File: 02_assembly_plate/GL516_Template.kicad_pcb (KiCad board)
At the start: 2 copper layers, 304.4 x 98.8 mm, 87 parts, among them J1 Conn_01x02, SW1 SW_PUSH, SW10 SW_PUSH, SW11 SW_PUSH, SW12 SW_PUSH, SW13 SW_PUSH, SW14 SW_PUSH, SW15 SW_PUSH, SW16 SW_PUSH, SW17 SW_PUSH, SW18 SW_PUSH, SW19 SW_PUSH, SW2 SW_PUSH, SW20 SW_PUSH, SW21 SW_PUSH, SW22 SW_PUSH, SW23 SW_PUSH, SW24 SW_PUSH, SW25 SW_PUSH, SW26 SW_PUSH, SW27 SW_PUSH, SW28 SW_PUSH, SW29 SW_PUSH, SW3 SW_PUSH, SW30 SW_PUSH, SW31 SW_PUSH, SW32 SW_PUSH, SW33 SW_PUSH, SW34 SW_PUSH, SW35 SW_PUSH, SW36 SW_PUSH, SW37 SW_PUSH, SW38 SW_PUSH, SW39 SW_PUSH, SW4 SW_PUSH, SW40 SW_PUSH, SW41 SW_PUSH, SW42 SW_PUSH, SW43 SW_PUSH, SW5 SW_PUSH, SW6 SW_PUSH, SW7 SW_PUSH, SW8 SW_PUSH, SW9 SW_PUSH, U1 BLEMicroPro

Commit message: fix wiring
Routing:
- net GND: track 51.2 -> 115.7 mm
- net Col1: track 389.0 -> 393.3 mm
- net Col0: track 409.8 -> 407.7 mm
- net Row1: track 468.5 -> 470.5 mm
- net Net-(D9-Pad2): track 7.82 -> 9.86 mm
- net Row0: track 431.7 -> 432.8 mm, vias 1 -> 0
- net Col6: track 316.5 -> 315.5 mm

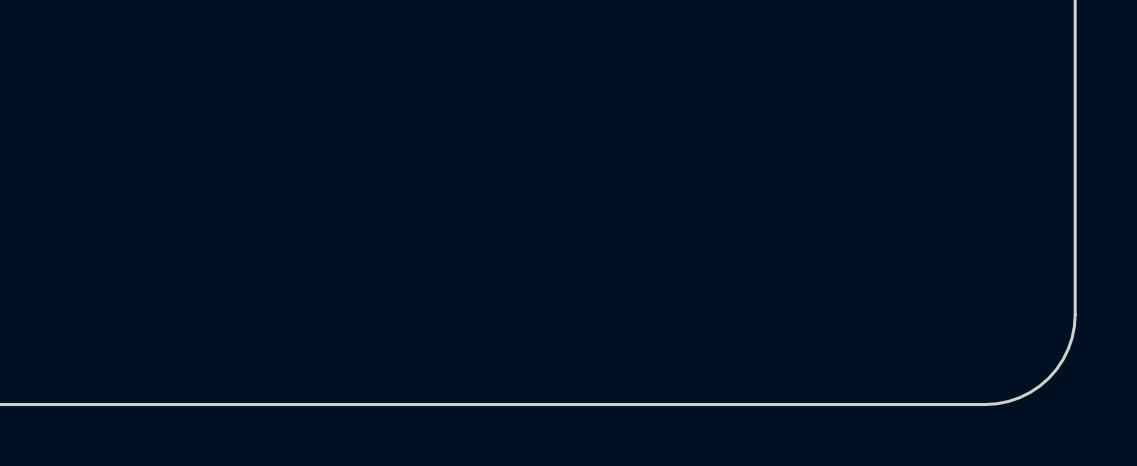
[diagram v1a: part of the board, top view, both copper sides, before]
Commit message: add version text on both Top and Assembly Plates
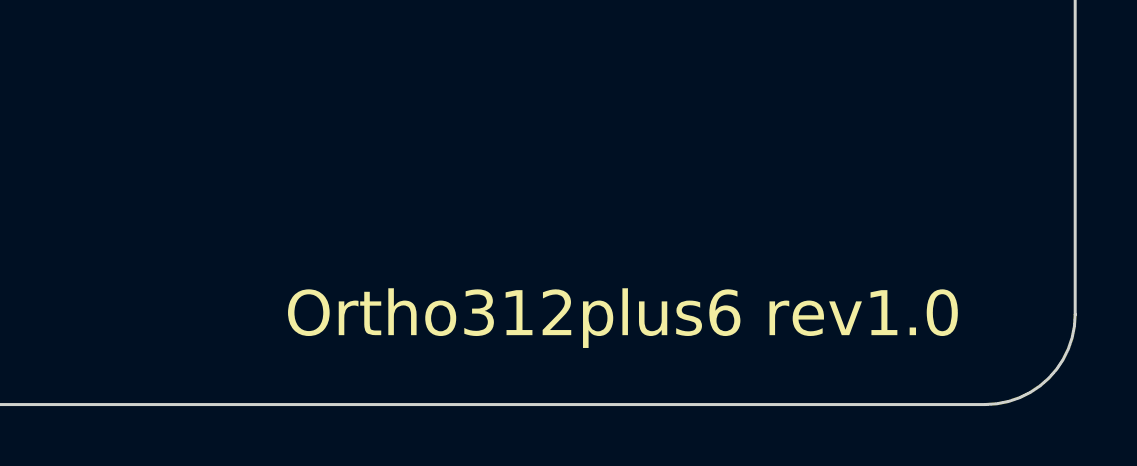
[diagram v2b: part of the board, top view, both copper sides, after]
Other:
- board text added: "Ortho312plus6 rev1.0"

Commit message: add battery + - silk / mod version
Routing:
- net Col1: track 393.3 -> 389.0 mm
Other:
- board text added: "+"
- board text added: "-"
- board text added: "Ortho312plus6 rev0.1"
- board text removed: "Ortho312plus6 rev1.0"
